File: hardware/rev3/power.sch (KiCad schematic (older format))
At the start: 15 parts, among them J1 USB_B, U1 LD1117S33TR

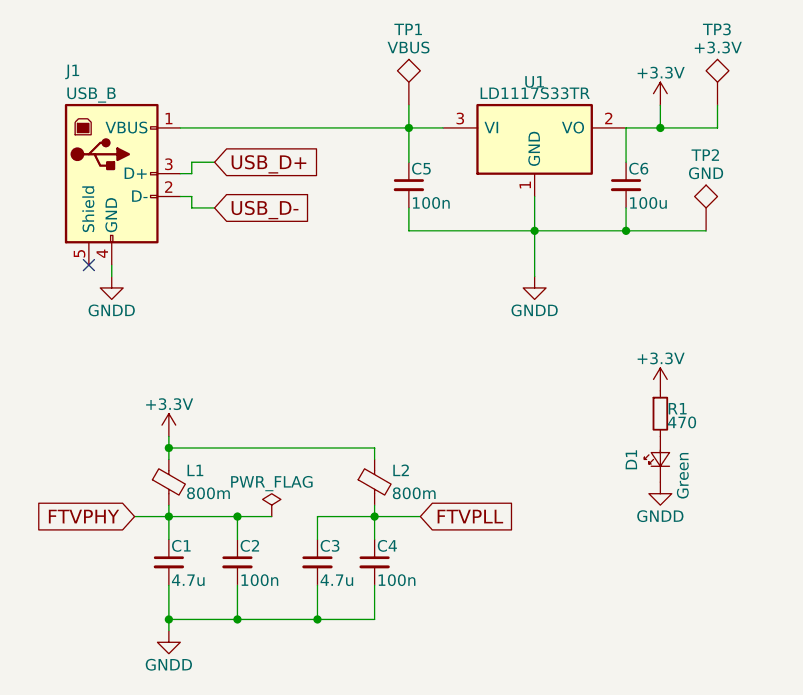
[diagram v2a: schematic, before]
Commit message: Finish up output amp schematic.
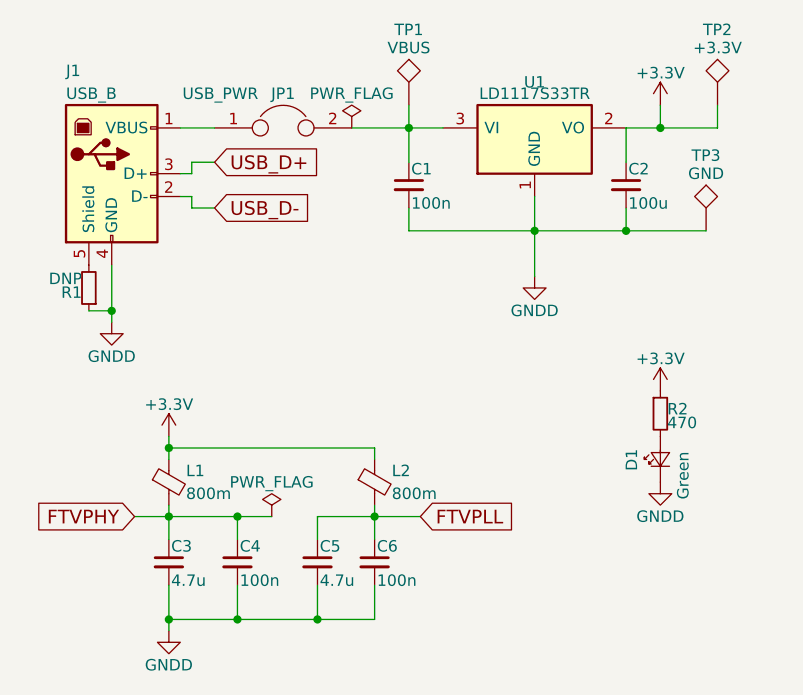
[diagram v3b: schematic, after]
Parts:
- added JP1: USB_PWR, symbol Jumper
- added R1: DNP, Resistors_SMD:R_0805, symbol R_Small
- renumbered C5 to C1, C6 to C2, C1 to C3, C2 to C4, C3 to C5, C4 to C6, R1 to R2, TP3 to TP2, TP2 to TP3
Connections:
- net GNDD: now also R1.1
- net at C1.1, TP1.1, U1.3 (VI): now also JP1.2; no longer J1.1 (VBUS)
- net at J1.5 (Shield): now also R1.2
- new net: J1.1 (VBUS), JP1.1
- no-connect marks 1 -> 0
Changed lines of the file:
@@
 LIBS:linear
 LIBS:ltc6409
+LIBS:ltc6269
 LIBS:rev3-cache
 EELAYER 25 0
@@
 Wire Wire Line
 	4700 3350 4700 3600
-Wire Wire Line
-	3700 3450 4850 3450
-$Comp
-L C_Small C5
+$Comp
+L C_Small C1
 U 1 1 58FAED12
 P 4700 3700
-F 0 "C5" H 4710 3770 50  0000 L CNN
+F 0 "C1" H 4710 3770 50  0000 L CNN
 F 1 "100n" H 4710 3620 50  0000 L CNN
 F 2 "Capacitors_SMD:C_0805" H 4700 3700 50  0001 C CNN
@@
 	5250 3750 5250 4100
 $Comp
-L C_Small C6
+L C_Small C2
 U 1 1 58FAEDEB
 P 5650 3700
-F 0 "C6" H 5660 3770 50  0000 L CNN
+F 0 "C2" H 5660 3770 50  0000 L CNN
 F 1 "100u" H 5660 3620 50  0000 L CNN
 F 2 "Capacitors_SMD:C_0805" H 5650 3700 50  0001 C CNN
@@
 $EndComp
 $Comp
-L TEST TP3
+L TEST TP2
 U 1 1 58FAEFA0
 P 6050 3350
-F 0 "TP3" H 6050 3650 50  0000 C BNN
+F 0 "TP2" H 6050 3650 50  0000 C BNN
 F 1 "+3.3V" H 6050 3600 50  0000 C CNN
 F 2 "Measurement_Points:Test_Point_Keystone_5005-5009_Compact" H 6050 3350 50  0001 C CNN
@@
 	1    0    0    -1
 $EndComp
-NoConn ~ 3300 4050
 $Comp
 L GNDD #PWR03
 U 1 1 58FAF242
-P 3400 4100
-F 0 "#PWR03" H 3400 3850 50  0001 C CNN
-F 1 "GNDD" H 3400 3950 50  0000 C CNN
-F 2 "" H 3400 4100 50  0001 C CNN
-F 3 "" H 3400 4100 50  0001 C CNN
-	1    3400 4100
-	1    0    0    -1
-$EndComp
-Wire Wire Line
-	3400 4050 3400 4100
+P 3400 4300
+F 0 "#PWR03" H 3400 4050 50  0001 C CNN
+F 1 "GNDD" H 3400 4150 50  0000 C CNN
+F 2 "" H 3400 4300 50  0001 C CNN
+F 3 "" H 3400 4300 50  0001 C CNN
+	1    3400 4300
+	1    0    0    -1
+$EndComp
+Wire Wire Line
+	3400 4050 3400 4300
 Text GLabel 3850 3600 2    60   Input ~ 0
 USB_D+
@@
 	3750 3600 3850 3600
 $Comp
-L TEST TP2
+L TEST TP3
 U 1 1 58FAF6C3
 P 6000 3900
-F 0 "TP2" H 6000 4200 50  0000 C BNN
+F 0 "TP3" H 6000 4200 50  0000 C BNN
 F 1 "GND" H 6000 4150 50  0000 C CNN
 F 2 "Measurement_Points:Test_Point_Keystone_5005-5009_Compact" H 6000 3900 50  0001 C CNN
@@
 $EndComp
 $Comp
-L C_Small C1
+L C_Small C3
 U 1 1 58FAFDBA
 P 3650 5350
-F 0 "C1" H 3660 5420 50  0000 L CNN
+F 0 "C3" H 3660 5420 50  0000 L CNN
 F 1 "4.7u" H 3660 5270 50  0000 L CNN
 F 2 "Capacitors_SMD:C_0805" H 3650 5350 50  0001 C CNN
@@
 $EndComp
 $Comp
-L C_Small C2
+L C_Small C4
 U 1 1 58FB0149
 P 3950 5350
-F 0 "C2" H 3960 5420 50  0000 L CNN
+F 0 "C4" H 3960 5420 50  0000 L CNN
 F 1 "100n" H 3960 5270 50  0000 L CNN
 F 2 "Capacitors_SMD:C_0805" H 3950 5350 50  0001 C CNN
@@
 $EndComp
 $Comp
-L C_Small C3
+L C_Small C5
 U 1 1 58FB098C
 P 4300 5350
-F 0 "C3" H 4310 5420 50  0000 L CNN
+F 0 "C5" H 4310 5420 50  0000 L CNN
 F 1 "4.7u" H 4310 5270 50  0000 L CNN
 F 2 "Capacitors_SMD:C_0805" H 4300 5350 50  0001 C CNN
@@
 $EndComp
 $Comp
-L C_Small C4
+L C_Small C6
 U 1 1 58FB0A55
 P 4550 5350
-F 0 "C4" H 4560 5420 50  0000 L CNN
+F 0 "C6" H 4560 5420 50  0000 L CNN
 F 1 "100n" H 4560 5270 50  0000 L CNN
 F 2 "Capacitors_SMD:C_0805" H 4550 5350 50  0001 C CNN
@@
 FTVPLL
 $Comp
-L R_Small R1
+L R_Small R2
 U 1 1 58FB807E
 P 5800 4700
-F 0 "R1" H 5830 4720 50  0000 L CNN
+F 0 "R2" H 5830 4720 50  0000 L CNN
 F 1 "470" H 5830 4660 50  0000 L CNN
 F 2 "Resistors_SMD:R_0805" H 5800 4700 50  0001 C CNN
@@
 $EndComp
 Connection ~ 3950 5150
+$Comp
+L R_Small R1
+U 1 1 5903E140
+P 3300 4150
+F 0 "R1" H 3330 4170 50  0000 L CNN
+F 1 "DNP" H 3330 4110 50  0000 L CNN
+F 2 "Resistors_SMD:R_0805" H 3300 4150 50  0001 C CNN
+F 3 "" H 3300 4150 50  0001 C CNN
+F 4 "P470ADCT-ND" H 3300 4150 60  0001 C CNN "DigiKey "
+	1    3300 4150
+	-1   0    0    1
+$EndComp
+Wire Wire Line
+	3300 4250 3400 4250
+Connection ~ 3400 4250
+$Comp
+L Jumper JP1
+U 1 1 5903FF4C
+P 4150 3450
+F 0 "JP1" H 4150 3600 50  0000 C CNN
+F 1 "USB_PWR" H 3875 3600 50  0000 C CNN
+F 2 "" H 4150 3450 50  0001 C CNN
+F 3 "" H 4150 3450 50  0001 C CNN
+	1    4150 3450
+	1    0    0    -1
+$EndComp
+Wire Wire Line
+	3700 3450 3850 3450
+Wire Wire Line
+	4450 3450 4850 3450
+$Comp
+L PWR_FLAG #FLG09
+U 1 1 59041176
+P 4450 3450
+F 0 "#FLG09" H 4450 3525 50  0001 C CNN
+F 1 "PWR_FLAG" H 4450 3600 50  0000 C CNN
+F 2 "" H 4450 3450 50  0001 C CNN
+F 3 "" H 4450 3450 50  0001 C CNN
+	1    4450 3450
+	1    0    0    -1
+$EndComp
 $EndSCHEMATC

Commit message: Add missing footprints.
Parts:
- C1, C2, C3, C4, C5, C6: footprint Capacitors_SMD:C_0805 -> Capacitors_SMD:C_0603_HandSoldering
- JP1: footprint (none) -> Pin_Headers:Pin_Header_Straight_1x02_Pitch2.54mm
- L1, L2: footprint Inductors_SMD:L_0805 -> Inductors_SMD:L_0603_HandSoldering
- R1, R2: footprint Resistors_SMD:R_0805 -> Resistors_SMD:R_0603_HandSoldering
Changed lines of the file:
@@
 F 0 "C1" H 4710 3770 50  0000 L CNN
 F 1 "100n" H 4710 3620 50  0000 L CNN
-F 2 "Capacitors_SMD:C_0805" H 4700 3700 50  0001 C CNN
+F 2 "Capacitors_SMD:C_0603_HandSoldering" H 4700 3700 50  0001 C CNN
 F 3 "" H 4700 3700 50  0001 C CNN
 F 4 "478-1395-1-ND" H 4700 3700 60  0001 C CNN "DigiKey"
@@
 F 0 "C2" H 5660 3770 50  0000 L CNN
 F 1 "100u" H 5660 3620 50  0000 L CNN
-F 2 "Capacitors_SMD:C_0805" H 5650 3700 50  0001 C CNN
+F 2 "Capacitors_SMD:C_0603_HandSoldering" H 5650 3700 50  0001 C CNN
 F 3 "" H 5650 3700 50  0001 C CNN
 F 4 "478-10568-1-ND" H 5650 3700 60  0001 C CNN "DigiKey"
@@
 F 0 "L1" H 3725 5050 50  0000 L CNN
 F 1 "800m" H 3725 4950 50  0000 L CNN
-F 2 "Inductors_SMD:L_0805" V 3580 5000 50  0001 C CNN
+F 2 "Inductors_SMD:L_0603_HandSoldering" V 3580 5000 50  0001 C CNN
 F 3 "" H 3650 5000 50  0001 C CNN
 F 4 "490-1054-1-ND" H 3650 5000 60  0001 C CNN "DigiKey"
@@
 F 0 "C3" H 3660 5420 50  0000 L CNN
 F 1 "4.7u" H 3660 5270 50  0000 L CNN
-F 2 "Capacitors_SMD:C_0805" H 3650 5350 50  0001 C CNN
+F 2 "Capacitors_SMD:C_0603_HandSoldering" H 3650 5350 50  0001 C CNN
 F 3 "" H 3650 5350 50  0001 C CNN
 F 4 "478-1415-1-ND" H 3650 5350 60  0001 C CNN "DigiKey"
@@
 F 0 "C4" H 3960 5420 50  0000 L CNN
 F 1 "100n" H 3960 5270 50  0000 L CNN
-F 2 "Capacitors_SMD:C_0805" H 3950 5350 50  0001 C CNN
+F 2 "Capacitors_SMD:C_0603_HandSoldering" H 3950 5350 50  0001 C CNN
 F 3 "" H 3950 5350 50  0001 C CNN
 F 4 "478-1395-1-ND" H 3950 5350 60  0001 C CNN "DigiKey"
@@
 F 0 "L2" H 4625 5050 50  0000 L CNN
 F 1 "800m" H 4625 4950 50  0000 L CNN
-F 2 "Inductors_SMD:L_0805" V 4480 5000 50  0001 C CNN
+F 2 "Inductors_SMD:L_0603_HandSoldering" V 4480 5000 50  0001 C CNN
 F 3 "" H 4550 5000 50  0001 C CNN
 F 4 "490-1054-1-ND" H 4550 5000 60  0001 C CNN "DigiKey"
@@
 F 0 "C5" H 4310 5420 50  0000 L CNN
 F 1 "4.7u" H 4310 5270 50  0000 L CNN
-F 2 "Capacitors_SMD:C_0805" H 4300 5350 50  0001 C CNN
+F 2 "Capacitors_SMD:C_0603_HandSoldering" H 4300 5350 50  0001 C CNN
 F 3 "" H 4300 5350 50  0001 C CNN
 F 4 "478-1415-1-ND" H 4300 5350 60  0001 C CNN "DigiKey"
@@
 F 0 "C6" H 4560 5420 50  0000 L CNN
 F 1 "100n" H 4560 5270 50  0000 L CNN
-F 2 "Capacitors_SMD:C_0805" H 4550 5350 50  0001 C CNN
+F 2 "Capacitors_SMD:C_0603_HandSoldering" H 4550 5350 50  0001 C CNN
 F 3 "" H 4550 5350 50  0001 C CNN
 F 4 "478-1395-1-ND" H 4550 5350 60  0001 C CNN "DigiKey"
@@
 F 0 "R2" H 5830 4720 50  0000 L CNN
 F 1 "470" H 5830 4660 50  0000 L CNN
-F 2 "Resistors_SMD:R_0805" H 5800 4700 50  0001 C CNN
+F 2 "Resistors_SMD:R_0603_HandSoldering" H 5800 4700 50  0001 C CNN
 F 3 "" H 5800 4700 50  0001 C CNN
 F 4 "P470ADCT-ND" H 5800 4700 60  0001 C CNN "DigiKey "
@@
 F 0 "R1" H 3330 4170 50  0000 L CNN
 F 1 "DNP" H 3330 4110 50  0000 L CNN
-F 2 "Resistors_SMD:R_0805" H 3300 4150 50  0001 C CNN
+F 2 "Resistors_SMD:R_0603_HandSoldering" H 3300 4150 50  0001 C CNN
 F 3 "" H 3300 4150 50  0001 C CNN
 F 4 "P470ADCT-ND" H 3300 4150 60  0001 C CNN "DigiKey "
@@
 F 0 "JP1" H 4150 3600 50  0000 C CNN
 F 1 "USB_PWR" H 3875 3600 50  0000 C CNN
-F 2 "" H 4150 3450 50  0001 C CNN
+F 2 "Pin_Headers:Pin_Header_Straight_1x02_Pitch2.54mm" H 4150 3450 50  0001 C CNN
 F 3 "" H 4150 3450 50  0001 C CNN
 	1    4150 3450

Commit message: Make some progress on layout.
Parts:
- R1: DigiKey  P470ADCT-ND -> DNP
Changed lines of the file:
@@
 F 2 "Resistors_SMD:R_0603_HandSoldering" H 3300 4150 50  0001 C CNN
 F 3 "" H 3300 4150 50  0001 C CNN
-F 4 "P470ADCT-ND" H 3300 4150 60  0001 C CNN "DigiKey "
+F 4 "DNP" H 3300 4150 60  0001 C CNN "DigiKey "
 	1    3300 4150
 	-1   0    0    1

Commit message: Fixup vreg decoupling.
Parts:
- added C47: 100n, Capacitors_SMD:C_0603_HandSoldering, symbol C_Small
- C2: value 100u -> 10u
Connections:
- net +3V3: now also C47.1
- net GNDD: now also C47.2
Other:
- moved on the sheet: TP3
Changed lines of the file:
@@
 	4700 3800 4700 3900
 Wire Wire Line
-	4700 3900 6000 3900
+	4700 3900 6250 3900
 Wire Wire Line
 	5250 3750 5250 4100
@@
 P 5650 3700
 F 0 "C2" H 5660 3770 50  0000 L CNN
-F 1 "100u" H 5660 3620 50  0000 L CNN
+F 1 "10u" H 5660 3620 50  0000 L CNN
 F 2 "Capacitors_SMD:C_0603_HandSoldering" H 5650 3700 50  0001 C CNN
 F 3 "" H 5650 3700 50  0001 C CNN
@@
 L TEST TP3
 U 1 1 58FAF6C3
-P 6000 3900
-F 0 "TP3" H 6000 4200 50  0000 C BNN
-F 1 "GND" H 6000 4150 50  0000 C CNN
-F 2 "Measurement_Points:Test_Point_Keystone_5005-5009_Compact" H 6000 3900 50  0001 C CNN
-F 3 "" H 6000 3900 50  0001 C CNN
-F 4 "36-5006-ND" H 6000 3900 60  0001 C CNN "DigiKey"
-	1    6000 3900
+P 6250 3900
+F 0 "TP3" H 6250 4200 50  0000 C BNN
+F 1 "GND" H 6250 4150 50  0000 C CNN
+F 2 "Measurement_Points:Test_Point_Keystone_5005-5009_Compact" H 6250 3900 50  0001 C CNN
+F 3 "" H 6250 3900 50  0001 C CNN
+F 4 "36-5006-ND" H 6250 3900 60  0001 C CNN "DigiKey"
+	1    6250 3900
 	1    0    0    -1
 $EndComp
@@
 	1    0    0    -1
 $EndComp
+$Comp
+L C_Small C47
+U 1 1 59048465
+P 5850 3700
+F 0 "C47" H 5860 3770 50  0000 L CNN
+F 1 "100n" H 5860 3620 50  0000 L CNN
+F 2 "Capacitors_SMD:C_0603_HandSoldering" H 5850 3700 50  0001 C CNN
+F 3 "" H 5850 3700 50  0001 C CNN
+F 4 "478-1395-1-ND" H 5850 3700 60  0001 C CNN "DigiKey"
+	1    5850 3700
+	1    0    0    -1
+$EndComp
+Wire Wire Line
+	5850 3800 5850 3900
+Connection ~ 5850 3900
+Wire Wire Line
+	5850 3600 5850 3450
+Connection ~ 5850 3450
 $EndSCHEMATC

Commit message: Update component selection based on digikey availability.
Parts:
- R2: value 470 -> 500
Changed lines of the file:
@@
 P 5800 4700
 F 0 "R2" H 5830 4720 50  0000 L CNN
-F 1 "470" H 5830 4660 50  0000 L CNN
+F 1 "500" H 5830 4660 50  0000 L CNN
 F 2 "Resistors_SMD:R_0603_HandSoldering" H 5800 4700 50  0001 C CNN
 F 3 "" H 5800 4700 50  0001 C CNN
